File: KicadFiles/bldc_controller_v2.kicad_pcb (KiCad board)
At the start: 2 copper layers, 50 x 89 mm, 184 parts, among them J1 Conn_01x05_Male, J10 Conn_01x02_Female, J11 Conn_01x02_Female, J12 Conn_01x02_Female, J13 Conn_01x02_Female, J14 Conn_01x02_Female, J15 Conn_01x04_Male, J2 Conn_01x03_Male, J3 Conn_01x03_Male, J4 1935174, J5 Conn_01x02_Female, J9 Conn_01x02_Female, Q1 DMN65D8L-7, Q10 IRLB8721PBF, Q11 IRLB8721PBF, Q2 DMN65D8L-7, Q3 DMN65D8L-7, Q4 DMN65D8L-7, Q5 IRF4905, Q6 IRLB8721PBF, Q7 IRLB8721PBF, Q8 IRLB8721PBF, Q9 IRLB8721PBF, SW2 D6C40 F1 LFS, SW3 1301.9314, SW4 1301.9314, SW5 SW_Push_DPDT, U1 ATmega328P-PU, U2 uA7810, U3 LM7805_TO220, U4 MCP601-xP, U5 LM339, U6 IRS2004, U7 IRS2004, U8 IRS2004, U9 HCPL-181-00DE, Y1 9B-16.000MBBK-B

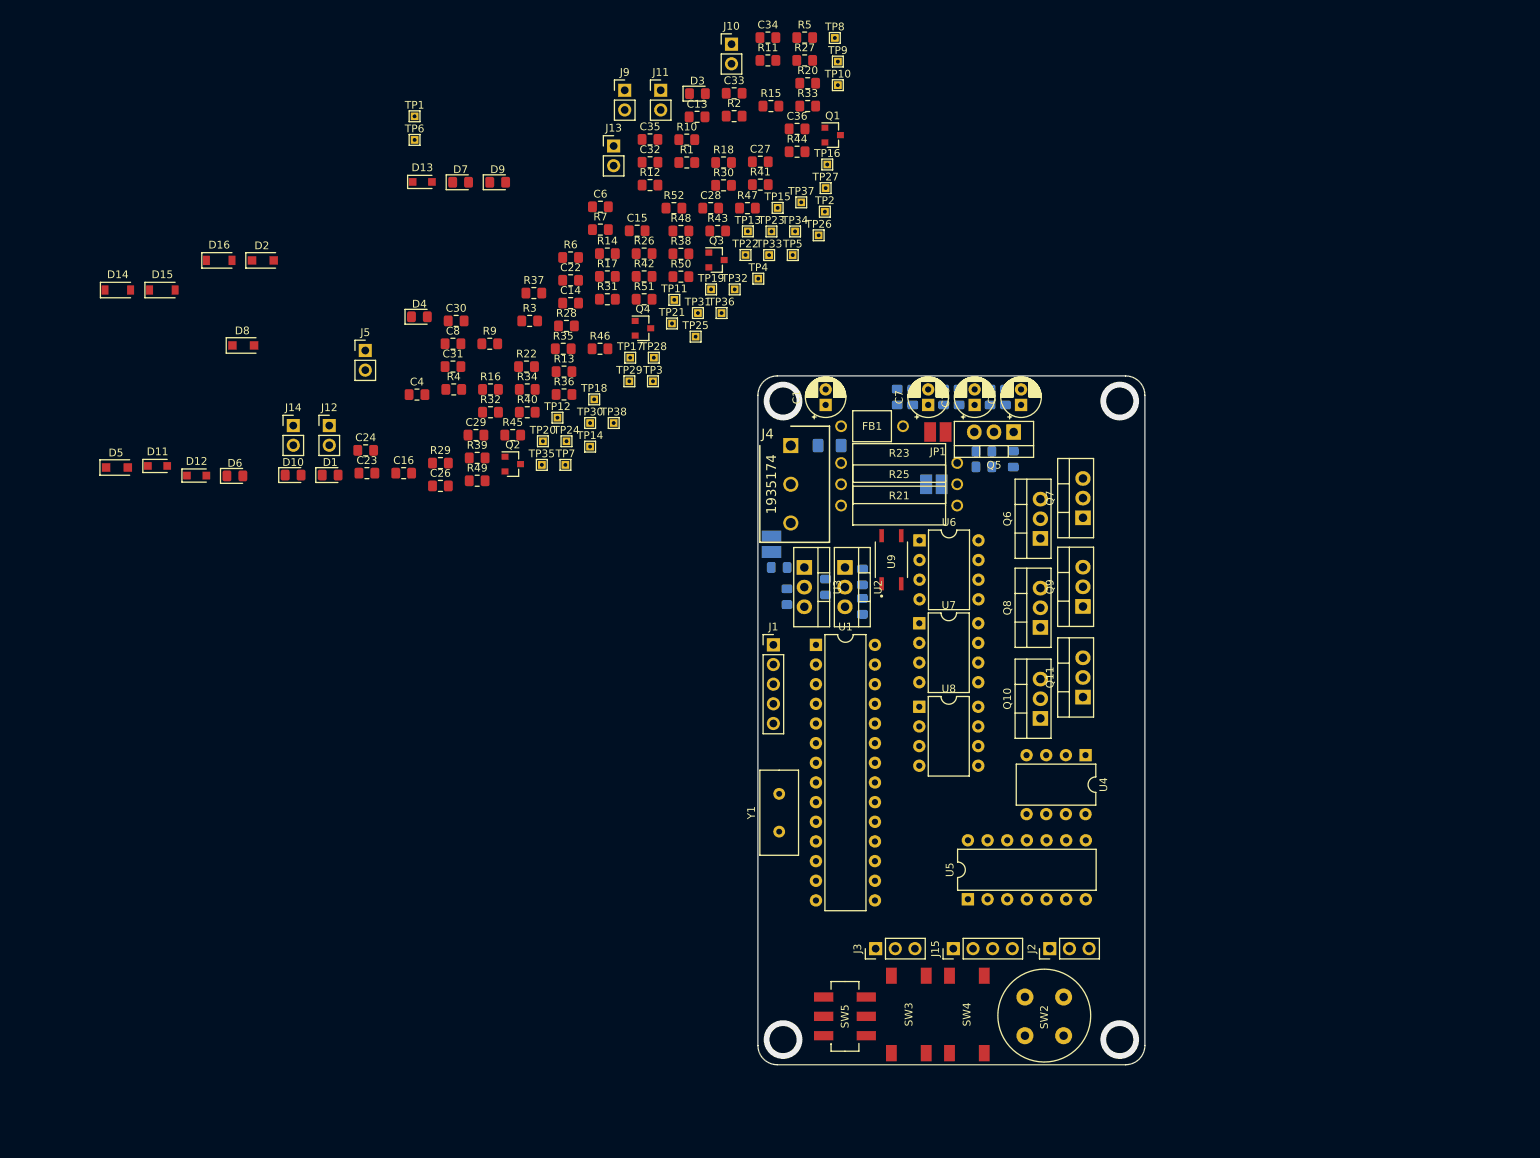
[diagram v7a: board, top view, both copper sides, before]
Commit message: Updated FET Placement
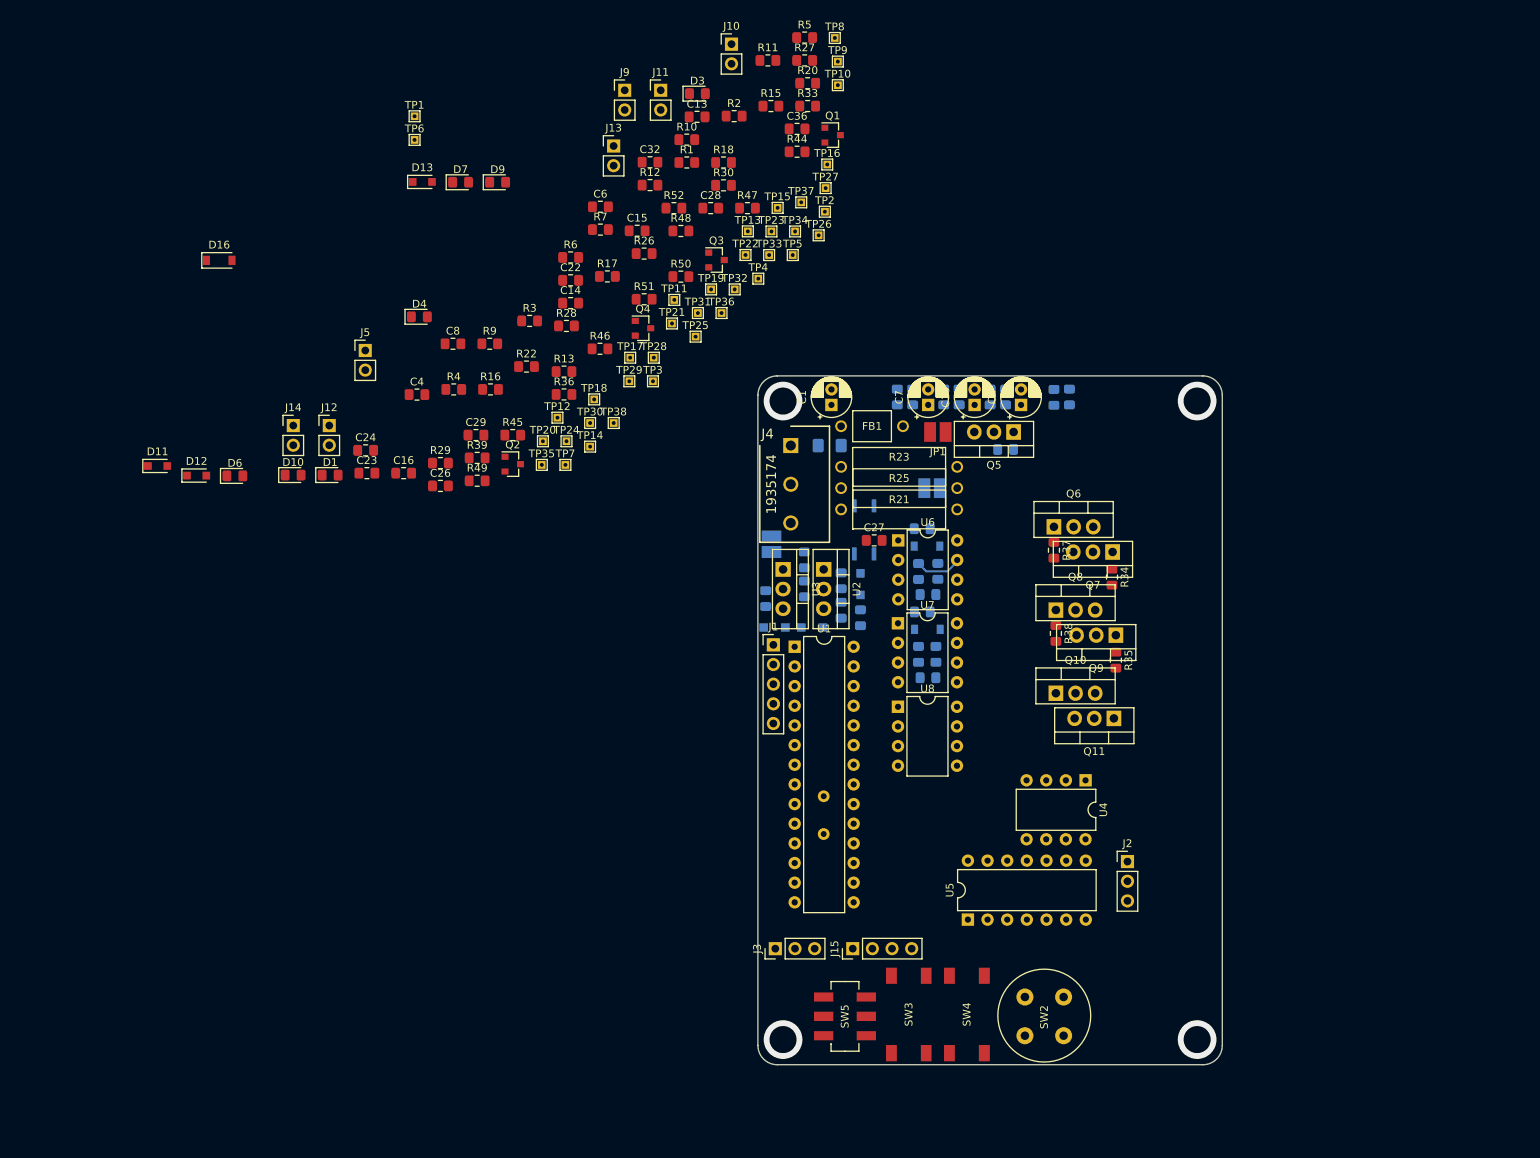
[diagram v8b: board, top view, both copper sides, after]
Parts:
- removed C33, C34, C35: 1uF, Capacitor_SMD:C_0805_2012Metric_Pad1.15x1.40mm_HandSolder
- C30, C31, D14, D15, D2, D5, D8, R14, R31, R32, R40, R41, R42, R43, U9, Y1: moved to B.Cu
- moved D14 109.7 mm to (134.8, 83.0), turned to 180 degrees
- moved D15 108.1 mm to (134.9, 93.8), turned to 180 degrees
- moved D5 92.2 mm to (120.0, 93.5), turned to 180 degrees
- moved D2 87.8 mm to (126.2, 87.9), turned to 270 degrees
- moved R35 82.0 mm to (159.2, 97.7), turned to 270 degrees
- moved R34 79.3 mm to (158.8, 87.0), turned to 270 degrees
- moved D8 77.7 mm to (115.2, 93.5), turned to 180 degrees
- moved R37 75.0 mm to (151.2, 83.5), turned to 270 degrees
- moved C31 72.6 mm to (136.0, 97.0), turned to 270 degrees
- moved C30 70.1 mm to (136.2, 86.2), turned to 270 degrees
- moved R38 68.9 mm to (151.5, 94.3), turned to 270 degrees
- moved R43 63.8 mm to (135.0, 100.0)
- moved R32 61.5 mm to (134.2, 91.5), turned to 180 degrees
- moved R42 60.3 mm to (133.8, 97.0), turned to 270 degrees
- moved R14 57.3 mm to (126.2, 92.2), turned to 270 degrees
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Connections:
- R40 pad 1: /GATE_A_HI -> Net-(R37-Pad2)
- R41 pad 1: /GATE_A_LO -> Net-(R34-Pad2)
- R42 pad 1: /GATE_B_HI -> Net-(R38-Pad2)
- R43 pad 1: /GATE_B_LO -> GNDD
- R43 pad 2: GNDD -> Net-(R35-Pad2)
- R44 pad 1: /GATE_C_HI -> GNDD
- R44 pad 2: GNDD -> Net-(R39-Pad2)
- R45 pad 1: /GATE_C_LO -> Net-(R36-Pad2)
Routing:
- net Net-(R37-Pad2): track 0.00 -> 6.14 mm
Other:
- board size 50 x 89 mm -> 60 x 89 mm
